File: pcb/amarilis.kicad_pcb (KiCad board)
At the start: 2 copper layers, 0 parts

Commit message: schematics done
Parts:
- added RZ1: RP2040-Zero, RP2040-Zero-Kicad:RP2040-Zero, F.Cu at (134.0, 71.9)
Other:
- board outline added: 94.8 x 44.2 mm
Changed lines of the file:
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@@
   )
   (net 0 "")
+  (net 1 "unconnected-(RZ1-Pad1)")
+  (net 2 "unconnected-(RZ1-Pad2)")
+  (net 3 "unconnected-(RZ1-Pad3)")
+  (net 4 "unconnected-(RZ1-Pad4)")
+  (net 5 "unconnected-(RZ1-Pad5)")
+  (net 6 "unconnected-(RZ1-Pad6)")
+  (net 7 "unconnected-(RZ1-Pad7)")
+  (net 8 "unconnected-(RZ1-Pad8)")
+  (net 9 "unconnected-(RZ1-Pad9)")
+  (net 10 "unconnected-(RZ1-Pad10)")
+  (net 11 "unconnected-(RZ1-Pad11)")
+  (net 12 "unconnected-(RZ1-Pad12)")
+  (net 13 "unconnected-(RZ1-Pad13)")
+  (net 14 "unconnected-(RZ1-Pad14)")
+  (net 15 "unconnected-(RZ1-Pad15)")
+  (net 16 "unconnected-(RZ1-Pad16)")
+  (net 17 "unconnected-(RZ1-Pad17)")
+  (net 18 "unconnected-(RZ1-Pad18)")
+  (net 19 "unconnected-(RZ1-Pad19)")
+  (net 20 "unconnected-(RZ1-Pad20)")
+  (net 21 "unconnected-(RZ1-Pad21)")
+  (net 22 "unconnected-(RZ1-Pad22)")
+  (net 23 "unconnected-(RZ1-Pad23)")
+  (footprint "RP2040-Zero-Kicad:RP2040-Zero" (layer "F.Cu")
+    (at 134.035 71.875)
+    (property "Sheetfile" "amarilis.kicad_sch")
+    (property "Sheetname" "")
+    (attr through_hole)
+    (fp_text reference "RZ1" (at 10.16 -15.45 unlocked) (layer "F.Fab")
+      (effects (font (size 1 1) (thickness 0.15)))
+    )
+    (fp_text value "RP2040-Zero" (at 10.16 -13.45 unlocked) (layer "F.SilkS")
+      (effects (font (size 1 1) (thickness 0.15)))
+    )
+    (fp_text user "${REFERENCE}" (at 10.16 -11.45 unlocked) (layer "F.Fab")
+      (effects (font (size 1 1) (thickness 0.15)))
+    )
+    (fp_line (start 1.16 -24.45) (end 1.16 -0.95) (layer "F.SilkS") (width 0.12))
+    (fp_line (start 19.16 -0.95) (end 19.16 -24.45) (layer "F.SilkS") (width 0.12))
+    (fp_line (start 1.16 -0.95) (end 19.16 -0.95) (layer "F.SilkS") (width 0.12))
+    (fp_line (start 19.16 -24.45) (end 1.16 -24.45) (layer "F.SilkS") (width 0.12))
+    (fp_line (start 19.16 -0.95) (end 1.16 -0.95) (layer "F.CrtYd") (width 0.05))
+    (fp_line (start 1.16 -0.95) (end 1.16 -24.45) (layer "F.CrtYd") (width 0.05))
+    (fp_line (start 19.16 -24.45) (end 19.16 -0.95) (layer "F.CrtYd") (width 0.05))
+    (fp_line (start 1.16 -24.45) (end 19.16 -24.45) (layer "F.CrtYd") (width 0.05))
+    (fp_line (start 5.83 -25.45) (end 14.46 -25.45) (layer "F.Fab") (width 0.1))
+    (fp_line (start 5.83 -25.45) (end 5.83 -24.45) (layer "F.Fab") (width 0.1))
+    (fp_line (start 14.46 -25.45) (end 14.46 -24.45) (layer "F.Fab") (width 0.1))
+    (pad "1" thru_hole roundrect (at 17.78 -22.86) (size 2.6 1.6) (drill 0.8 (offset 0.6 0)) (layers *.Cu *.Mask) (roundrect_rratio 0.25)
+      (net 1 "unconnected-(RZ1-Pad1)") (pinfunction "GP0") (pintype "bidirectional"))
+    (pad "2" thru_hole roundrect (at 17.78 -20.32) (size 2.6 1.6) (drill 0.8 (offset 0.6 0)) (layers *.Cu *.Mask) (roundrect_rratio 0.25)
+      (net 2 "unconnected-(RZ1-Pad2)") (pinfunction "GP1") (pintype "bidirectional"))
+    (pad "3" thru_hole roundrect (at 17.78 -17.78) (size 2.6 1.6) (drill 0.8 (offset 0.6 0)) (layers *.Cu *.Mask) (roundrect_rratio 0.25)
+      (net 3 "unconnected-(RZ1-Pad3)") (pinfunction "GP2") (pintype "bidirectional"))
+    (pad "4" thru_hole roundrect (at 17.78 -15.24) (size 2.6 1.6) (drill 0.8 (offset 0.6 0)) (layers *.Cu *.Mask) (roundrect_rratio 0.25)
+      (net 4 "unconnected-(RZ1-Pad4)") (pinfunction "GP3") (pintype "bidirectional"))
+    (pad "5" thru_hole roundrect (at 17.78 -12.7) (size 2.6 1.6) (drill 0.8 (offset 0.6 0)) (layers *.Cu *.Mask) (roundrect_rratio 0.25)
+      (net 5 "unconnected-(RZ1-Pad5)") (pinfunction "GP4") (pintype "bidirectional"))
+    (pad "6" thru_hole roundrect (at 17.78 -10.16) (size 2.6 1.6002) (drill 0.8 (offset 0.6 0)) (layers *.Cu *.Mask) (roundrect_rratio 0.25)
+      (net 6 "unconnected-(RZ1-Pad6)") (pinfunction "GP5") (pintype "bidirectional"))
+    (pad "7" thru_hole roundrect (at 17.78 -7.62) (size 2.6 1.6002) (drill 0.8 (offset 0.6 0)) (layers *.Cu *.Mask) (roundrect_rratio 0.25)
+      (net 7 "unconnected-(RZ1-Pad7)") (pinfunction "GP6") (pintype "bidirectional"))
+    (pad "8" thru_hole roundrect (at 17.78 -5.08) (size 2.6 1.6002) (drill 0.8 (offset 0.6 0)) (layers *.Cu *.Mask) (roundrect_rratio 0.25)
+      (net 8 "unconnected-(RZ1-Pad8)") (pinfunction "GP7") (pintype "bidirectional"))
+    (pad "9" thru_hole roundrect (at 17.78 -2.54) (size 2.6 1.6002) (drill 0.8 (offset 0.6 0)) (layers *.Cu *.Mask) (roundrect_rratio 0.25)
+      (net 9 "unconnected-(RZ1-Pad9)") (pinfunction "GP8") (pintype "bidirectional"))
+    (pad "10" thru_hole roundrect (at 15.24 -2.33) (size 1.6 2.6) (drill 0.8 (offset 0 0.6)) (layers *.Cu *.Mask) (roundrect_rratio 0.25)
+      (net 10 "unconnected-(RZ1-Pad10)") (pinfunction "GP9") (pintype "bidirectional"))
+    (pad "11" thru_hole roundrect (at 12.7 -2.33) (size 1.5748 2.6) (drill 0.8 (offset 0 0.6)) (layers *.Cu *.Mask) (roundrect_rratio 0.25)
+      (net 11 "unconnected-(RZ1-Pad11)") (pinfunction "GP10") (pintype "bidirectional"))
+    (pad "12" thru_hole roundrect (at 10.16 -2.33) (size 1.5748 2.6) (drill 0.8 (offset 0 0.6)) (layers *.Cu *.Mask) (roundrect_rratio 0.25)
+      (net 12 "unconnected-(RZ1-Pad12)") (pinfunction "GP11") (pintype "bidirectional"))
+    (pad "13" thru_hole roundrect (at 7.62 -2.33) (size 1.5748 2.6) (drill 0.8 (offset 0 0.6)) (layers *.Cu *.Mask) (roundrect_rratio 0.25)
+      (net 13 "unconnected-(RZ1-Pad13)") (pinfunction "GP12") (pintype "bidirectional"))
+    (pad "14" thru_hole roundrect (at 5.08 -2.33) (size 1.5748 2.6) (drill 0.8 (offset 0 0.6)) (layers *.Cu *.Mask) (roundrect_rratio 0.25)
+      (net 14 "unconnected-(RZ1-Pad14)") (pinfunction "GP13") (pintype "bidirectional"))
+    (pad "15" thru_hole roundrect (at 2.54 -2.54) (size 2.6 1.6002) (drill 0.8 (offset -0.6 0)) (layers *.Cu *.Mask) (roundrect_rratio 0.25)
+      (net 15 "unconnected-(RZ1-Pad15)") (pinfunction "GP14") (pintype "bidirectional"))
+    (pad "16" thru_hole roundrect (at 2.54 -5.08) (size 2.6 1.6002) (drill 0.8 (offset -0.6 0)) (layers *.Cu *.Mask) (roundrect_rratio 0.25)
+      (net 16 "unconnected-(RZ1-Pad16)") (pinfunction "GP15") (pintype "bidirectional"))
+    (pad "17" thru_hole roundrect (at 2.54 -7.62) (size 2.6 1.6002) (drill 0.8 (offset -0.6 0)) (layers *.Cu *.Mask) (roundrect_rratio 0.25)
+      (net 17 "unconnected-(RZ1-Pad17)") (pinfunction "GP26") (pintype "bidirectional"))
+    (pad "18" thru_hole roundrect (at 2.54 -10.16) (size 2.6 1.6002) (drill 0.8 (offset -0.6 0)) (layers *.Cu *.Mask) (roundrect_rratio 0.25)
+      (net 18 "unconnected-(RZ1-Pad18)") (pinfunction "GP27") (pintype "bidirectional"))
+    (pad "19" thru_hole roundrect (at 2.54 -22.86) (size 2.6 1.6002) (drill 0.8 (offset -0.6 0)) (layers *.Cu *.Mask) (roundrect_rratio 0.25)
+      (net 19 "unconnected-(RZ1-Pad19)") (pinfunction "GP28") (pintype "bidirectional"))
+    (pad "20" thru_hole roundrect (at 2.54 -20.32) (size 2.6 1.6002) (drill 0.8 (offset -0.6 0)) (layers *.Cu *.Mask) (roundrect_rratio 0.25)
+      (net 20 "unconnected-(RZ1-Pad20)") (pinfunction "GP29") (pintype "bidirectional"))
+    (pad "21" thru_hole roundrect (at 2.54 -17.78) (size 2.6 1.6002) (drill 0.8 (offset -0.6 0)) (layers *.Cu *.Mask) (roundrect_rratio 0.25)
+      (net 21 "unconnected-(RZ1-Pad21)") (pinfunction "3V3") (pintype "power_in"))
+    (pad "22" thru_hole roundrect (at 2.54 -12.7) (size 2.6 1.6002) (drill 0.8 (offset -0.6 0)) (layers *.Cu *.Mask) (roundrect_rratio 0.25)
+      (net 22 "unconnected-(RZ1-Pad22)") (pinfunction "5V") (pintype "power_in"))
+    (pad "23" thru_hole roundrect (at 2.54 -15.24) (size 2.6 1.6002) (drill 0.8 (offset -0.6 0)) (layers *.Cu *.Mask) (roundrect_rratio 0.25)
+      (net 23 "unconnected-(RZ1-Pad23)") (pinfunction "GND") (pintype "power_in"))
+  )
+  (gr_rect (start 95.75 36) (end 190.5 80.25) (layer "Edge.Cuts") (width 0.1) (fill none))
 )

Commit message: starting the PCB
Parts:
- added D1: 1N4148, kbd:D3_TH, F.Cu at (151.2, 75.2)
- added D10: 1N4148, kbd:D3_TH, F.Cu at (151.2, 77.6)
- added D11: 1N4148, kbd:D3_TH, F.Cu at (195.1, 70.5)
- added D12: 1N4148, kbd:D3_TH, F.Cu at (133.7, 77.6)
- added D13: 1N4148, kbd:D3_TH, F.Cu at (186.3, 70.5)
- added D14: 1N4148, kbd:D3_TH, F.Cu at (203.9, 75.2)
- added D15: 1N4148, kbd:D3_TH, F.Cu at (186.3, 75.2)
- added D16: 1N4148, kbd:D3_TH, F.Cu at (177.6, 75.2)
- added D17: 1N4148, kbd:D3_TH, F.Cu at (133.7, 70.5)
- added D18: 1N4148, kbd:D3_TH, F.Cu at (160.0, 77.6)
- added D19: 1N4148, kbd:D3_TH, F.Cu at (177.6, 72.9)
- added D2: 1N4148, kbd:D3_TH, F.Cu at (168.8, 70.5)
- added D20: 1N4148, kbd:D3_TH, F.Cu at (168.8, 75.2)
- added D21: 1N4148, kbd:D3_TH, F.Cu at (203.9, 70.5)
- added D22: 1N4148, kbd:D3_TH, F.Cu at (212.6, 70.5)
- added D23: 1N4148, kbd:D3_TH, F.Cu at (142.5, 72.9)
- added D24: 1N4148, kbd:D3_TH, F.Cu at (142.5, 70.5)
- added D25: 1N4148, kbd:D3_TH, F.Cu at (168.8, 72.9)
- added D26: 1N4148, kbd:D3_TH, F.Cu at (133.7, 75.2)
- added D27: 1N4148, kbd:D3_TH, F.Cu at (195.1, 75.2)
- added D28: 1N4148, kbd:D3_TH, F.Cu at (177.6, 70.5)
- added D29: 1N4148, kbd:D3_TH, F.Cu at (177.6, 77.6)
- added D3: 1N4148, kbd:D3_TH, F.Cu at (133.7, 72.9)
- added D30: 1N4148, kbd:D3_TH, F.Cu at (142.5, 75.2)
- added D31: 1N4148, kbd:D3_TH, F.Cu at (168.8, 77.6)
- added D32: 1N4148, kbd:D3_TH, F.Cu at (160.0, 70.5)
- added D33: 1N4148, kbd:D3_TH, F.Cu at (195.1, 77.6)
- added D34: 1N4148, kbd:D3_TH, F.Cu at (151.2, 70.5)
- added D35: 1N4148, kbd:D3_TH, F.Cu at (186.3, 72.9)
- added D36: 1N4148, kbd:D3_TH, F.Cu at (160.0, 72.9)
- added D4: 1N4148, kbd:D3_TH, F.Cu at (195.1, 72.9)
- added D5: 1N4148, kbd:D3_TH, F.Cu at (151.2, 72.9)
- added D6: 1N4148, kbd:D3_TH, F.Cu at (203.9, 72.9)
- added D7: 1N4148, kbd:D3_TH, F.Cu at (186.3, 77.6)
- added D8: 1N4148, kbd:D3_TH, F.Cu at (142.5, 77.6)
- added D9: 1N4148, kbd:D3_TH, F.Cu at (160.0, 75.2)
- added SW1: SW_PUSH, kbd:CherryMX_1u, F.Cu at (179.8, -21.6)
- added SW10: SW_PUSH, kbd:CherryMX_1u, F.Cu at (200.0, -21.6)
- added SW11: SW_PUSH, kbd:CherryMX_1u, F.Cu at (139.4, 18.8)
- added SW12: SW_PUSH, kbd:CherryMX_1u, F.Cu at (139.4, 39.0)
- added SW13: SW_PUSH, kbd:CherryMX_1u, F.Cu at (220.2, 59.2)
- added SW14: SW_PUSH, kbd:CherryMX_1u, F.Cu at (280.8, -1.43)
- added SW15: SW_PUSH, kbd:CherryMX_1u, F.Cu at (159.6, -21.6)
- added SW16: SW_PUSH, kbd:CherryMX_1u, F.Cu at (260.6, -1.43)
- added SW17: SW_PUSH, kbd:CherryMX_1u, F.Cu at (159.6, 39.0)
- added SW18: SW_PUSH, kbd:CherryMX_1u, F.Cu at (159.6, 18.8)
- added SW19: SW_PUSH, kbd:CherryMX_1u, F.Cu at (200.0, 18.8)
- added SW2: SW_PUSH, kbd:CherryMX_1u, F.Cu at (139.4, -21.6)
- added SW20: SW_PUSH, kbd:CherryMX_1u, F.Cu at (220.2, -21.6)
- added SW21: SW_PUSH, kbd:CherryMX_1u, F.Cu at (301.0, -21.6)
- added SW22: SW_PUSH, kbd:CherryMX_1u, F.Cu at (179.8, 59.2)
- added SW23: SW_PUSH, kbd:CherryMX_1u, F.Cu at (159.6, -1.43)
- added SW24: SW_PUSH, kbd:CherryMX_1u, F.Cu at (139.4, -1.43)
- added SW25: SW_PUSH, kbd:CherryMX_1u, F.Cu at (159.6, 59.2)
- added SW26: SW_PUSH, kbd:CherryMX_1u, F.Cu at (179.8, 18.8)
- added SW27: SW_PUSH, kbd:CherryMX_1u, F.Cu at (260.6, -21.6)
- added SW28: SW_PUSH, kbd:CherryMX_1u, F.Cu at (220.2, 39.0)
- added SW29: SW_PUSH, kbd:CherryMX_1u, F.Cu at (200.0, -1.43)
- added SW3: SW_PUSH, kbd:CherryMX_1u, F.Cu at (240.4, 59.2)
- added SW30: SW_PUSH, kbd:CherryMX_1u, F.Cu at (220.2, -1.43)
- added SW31: SW_PUSH, kbd:CherryMX_1u, F.Cu at (179.8, 39.0)
- added SW32: SW_PUSH, kbd:CherryMX_1u, F.Cu at (260.6, 18.8)
- added SW33: SW_PUSH, kbd:CherryMX_1u, F.Cu at (139.4, 59.2)
- added SW34: SW_PUSH, kbd:CherryMX_1u, F.Cu at (240.4, 18.8)
- added SW35: SW_PUSH, kbd:CherryMX_1u, F.Cu at (220.2, 18.8)
- added SW36: SW_PUSH, kbd:CherryMX_1u, F.Cu at (200.0, 59.2)
- added SW4: SW_PUSH, kbd:CherryMX_1u, F.Cu at (240.4, -21.6)
- added SW5: SW_PUSH, kbd:CherryMX_1u, F.Cu at (240.4, -1.43)
- added SW6: SW_PUSH, kbd:CherryMX_1u, F.Cu at (179.8, -1.43)
- added SW7: SW_PUSH, kbd:CherryMX_1u, F.Cu at (200.0, 39.0)
- added SW8: SW_PUSH, kbd:CherryMX_1u, F.Cu at (280.8, -21.6)
- added SW9: SW_PUSH, kbd:CherryMX_1u, F.Cu at (240.4, 39.0)
- moved RZ1 103.6 mm to (77.0, -14.6)
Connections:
- RZ1 pad 1: unconnected-(RZ1-Pad1) -> COL0
- RZ1 pad 10: unconnected-(RZ1-Pad10) -> COL9
- RZ1 pad 11: unconnected-(RZ1-Pad11) -> ROW0
- RZ1 pad 12: unconnected-(RZ1-Pad12) -> ROW1
- RZ1 pad 13: unconnected-(RZ1-Pad13) -> ROW2
- RZ1 pad 14: unconnected-(RZ1-Pad14) -> ROW3
- RZ1 pad 2: unconnected-(RZ1-Pad2) -> COL1
- RZ1 pad 3: unconnected-(RZ1-Pad3) -> COL2
- RZ1 pad 4: unconnected-(RZ1-Pad4) -> COL3
- RZ1 pad 5: unconnected-(RZ1-Pad5) -> COL4
- RZ1 pad 6: unconnected-(RZ1-Pad6) -> COL5
- RZ1 pad 7: unconnected-(RZ1-Pad7) -> COL6
- RZ1 pad 8: unconnected-(RZ1-Pad8) -> COL7
- RZ1 pad 9: unconnected-(RZ1-Pad9) -> COL8
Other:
- board outline removed

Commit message: PCB ready!
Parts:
- moved SW21 289.0 mm to (41.0, 104.5), turned to -10 degrees
- moved SW32 205.0 mm to (92.9, 136.5), turned to -25 degrees
- moved SW14 199.9 mm to (101.9, 87.8), turned to -10 degrees
- moved SW4 162.7 mm to (105.2, 69.0), turned to -10 degrees
- moved SW1 159.2 mm to (47.6, 67.0), turned to -10 degrees
- moved SW3 153.3 mm to (87.2, 61.8), turned to -10 degrees
- moved SW27 142.9 mm to (197.4, 106.5), turned to 10 degrees
- moved SW5 139.2 mm to (123.7, 74.3), turned to -10 degrees
- moved SW13 138.0 mm to (83.9, 80.5), turned to -10 degrees
- moved SW34 137.1 mm to (185.9, 144.6), turned to 40 degrees
- moved SW31 128.3 mm to (85.1, 125.5), turned to -10 degrees
- moved SW23 128.0 mm to (80.6, 99.3), turned to -10 degrees
- moved SW16 127.0 mm to (175.7, 93.0), turned to 10 degrees
- moved SW22 125.5 mm to (61.1, 99.9), turned to -10 degrees
- moved SW15 121.2 mm to (120.4, 93.0), turned to -10 degrees
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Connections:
- RZ1 pad 1: COL0 -> unconnected-(RZ1-Pad1)
- RZ1 pad 10: COL9 -> unconnected-(RZ1-Pad10)
- RZ1 pad 15: unconnected-(RZ1-Pad15) -> COL4
- RZ1 pad 16: unconnected-(RZ1-Pad16) -> COL3
- RZ1 pad 17: unconnected-(RZ1-Pad17) -> COL2
- RZ1 pad 18: unconnected-(RZ1-Pad18) -> COL1
- RZ1 pad 2: COL1 -> unconnected-(RZ1-Pad2)
- RZ1 pad 22: unconnected-(RZ1-Pad22) -> COL0
- RZ1 pad 3: COL2 -> unconnected-(RZ1-Pad3)
- RZ1 pad 4: COL3 -> unconnected-(RZ1-Pad4)
- RZ1 pad 5: COL4 -> COL9
- RZ1 pad 6: COL5 -> COL8
- RZ1 pad 7: COL6 -> COL7
- RZ1 pad 8: COL7 -> COL6
- RZ1 pad 9: COL8 -> COL5
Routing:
- net COL0: track 0.00 -> 146.9 mm
- net COL9: track 0.00 -> 137.7 mm
- net COL2: track 0.00 -> 135.1 mm
- net Net-(D10-Pad2): track 0.00 -> 131.7 mm
- net COL7: track 0.00 -> 127.5 mm
- net Net-(D1-Pad2): track 0.00 -> 127.1 mm
- net COL1: track 0.00 -> 126.6 mm
- net Net-(D20-Pad2): track 0.00 -> 124.3 mm
- net Net-(D11-Pad2): track 0.00 -> 121.6 mm
- net Net-(D30-Pad2): track 0.00 -> 118.7 mm
- net COL8: track 0.00 -> 117.8 mm
- net COL3: track 0.00 -> 116.2 mm
- net Net-(D21-Pad2): track 0.00 -> 115.4 mm
- net COL6: track 0.00 -> 110.3 mm
- net Net-(D9-Pad2): track 0.00 -> 106.4 mm
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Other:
- board outline added: 239.7 x 113 mm

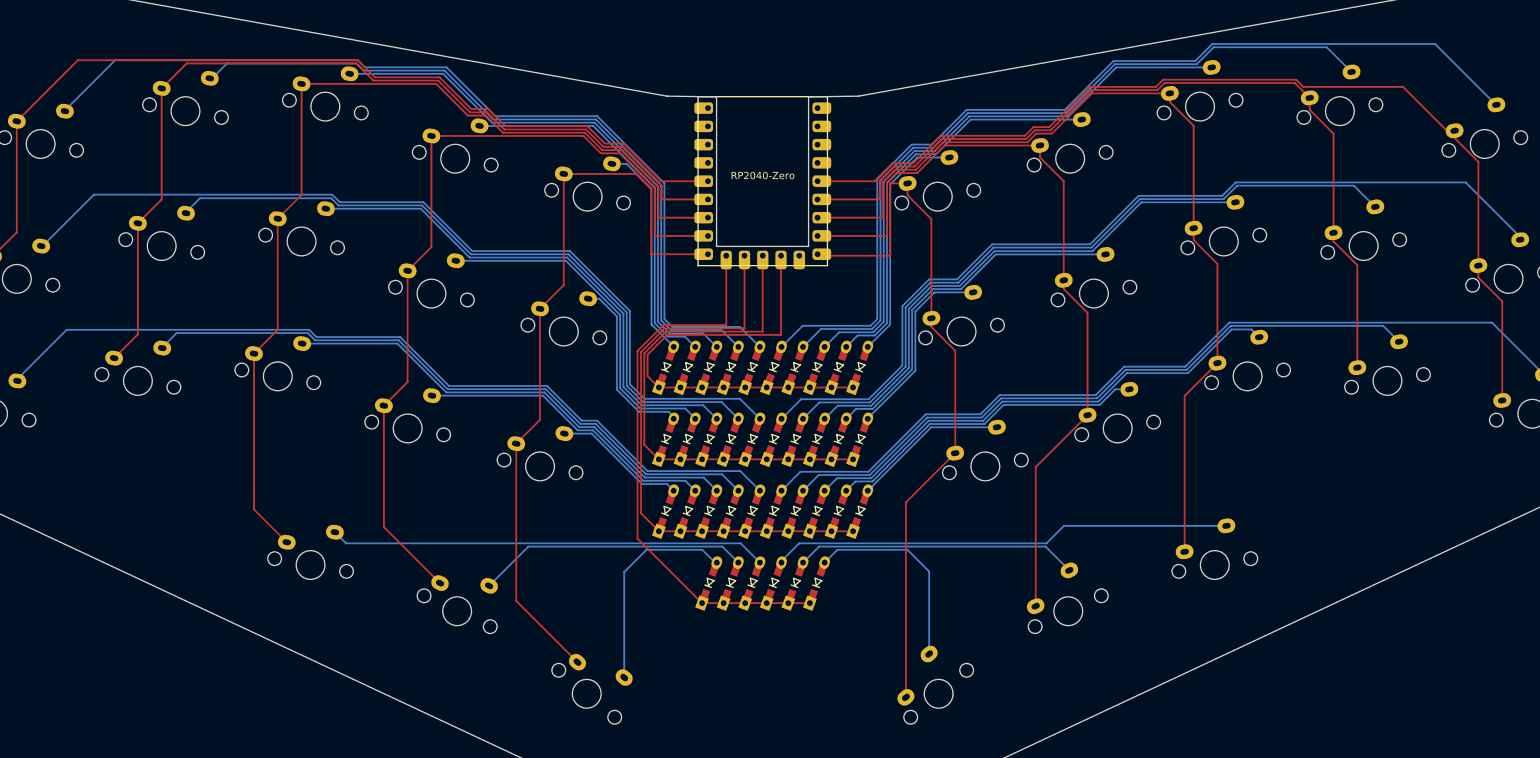
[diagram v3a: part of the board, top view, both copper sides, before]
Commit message: mounting holes + some traces adjustments
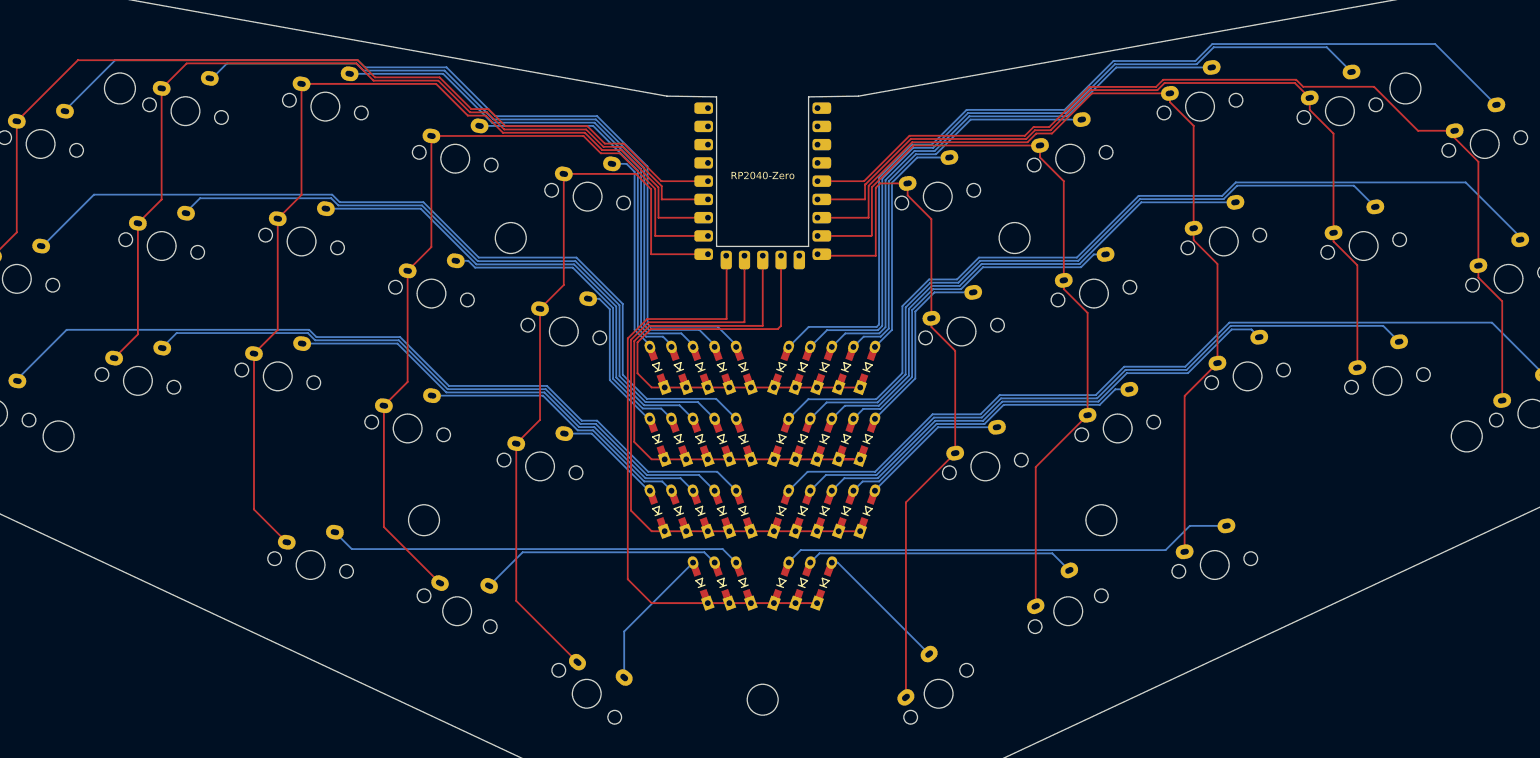
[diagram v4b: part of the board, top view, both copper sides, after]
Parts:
- added Ref**: Val**, kbd:spacer_m2, F.Cu at (183.1, 80.0)
- added Ref**: Val**, kbd:spacer_m2, F.Cu at (148.0, 144.3)
- added Ref**: Val**, kbd:spacer_m2, F.Cu at (195.1, 119.3)
- added Ref**: Val**, kbd:spacer_m2, F.Cu at (58.6, 59.2)
- added Ref**: Val**, kbd:spacer_m2, F.Cu at (237.4, 59.2)
- added Ref**: Val**, kbd:spacer_m2, F.Cu at (50.1, 107.6)
- added Ref**: Val**, kbd:spacer_m2, F.Cu at (100.9, 119.3)
- added Ref**: Val**, kbd:spacer_m2, F.Cu at (246.0, 107.6)
- added Ref**: Val**, kbd:spacer_m2, F.Cu at (113.0, 80.0)
- moved D1 1.25 mm to (145.4, 98.0), turned to 110 degrees
- moved D11 1.25 mm to (145.4, 108.0), turned to 110 degrees
- moved D12 1.25 mm to (142.4, 108.0), turned to 110 degrees
- moved D13 1.25 mm to (139.4, 108.0), turned to 110 degrees
- moved D14 1.25 mm to (136.4, 108.0), turned to 110 degrees
- moved D15 1.25 mm to (133.4, 108.0), turned to 110 degrees
- moved D2 1.25 mm to (142.4, 98.0), turned to 110 degrees
- moved D21 1.25 mm to (145.4, 118.0), turned to 110 degrees
- moved D22 1.25 mm to (142.4, 118.0), turned to 110 degrees
- moved D23 1.25 mm to (139.4, 118.0), turned to 110 degrees
- moved D24 1.25 mm to (136.4, 118.0), turned to 110 degrees
- moved D25 1.25 mm to (133.4, 118.0), turned to 110 degrees
- moved D3 1.25 mm to (139.4, 98.0), turned to 110 degrees
- moved D31 1.25 mm to (145.4, 128.0), turned to 110 degrees
- moved D32 1.25 mm to (142.4, 128.0), turned to 110 degrees
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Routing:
- net Net-(D34-Pad2): track 28.0 -> 18.8 mm
- net Net-(D33-Pad2): track 29.3 -> 20.5 mm
- net ROW3: track 77.3 -> 84.9 mm
- net ROW1: track 70.9 -> 77.0 mm
- net Net-(D32-Pad2): track 37.9 -> 33.9 mm
- net Net-(D12-Pad2): track 96.3 -> 92.8 mm
- net Net-(D11-Pad2): track 121.6 -> 118.1 mm
- net Net-(D13-Pad2): track 72.4 -> 69.0 mm
- net Net-(D14-Pad2): track 48.4 -> 44.9 mm
- net Net-(D15-Pad2): track 24.7 -> 21.3 mm
- net Net-(D23-Pad2): track 66.2 -> 62.9 mm
- net Net-(D31-Pad2): track 60.9 -> 57.6 mm
- net Net-(D25-Pad2): track 18.5 -> 15.2 mm
- net Net-(D24-Pad2): track 42.1 -> 38.8 mm
- net Net-(D22-Pad2): track 90.1 -> 86.7 mm
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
